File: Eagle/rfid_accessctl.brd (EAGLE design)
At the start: 50 x 40 mm, 21 parts

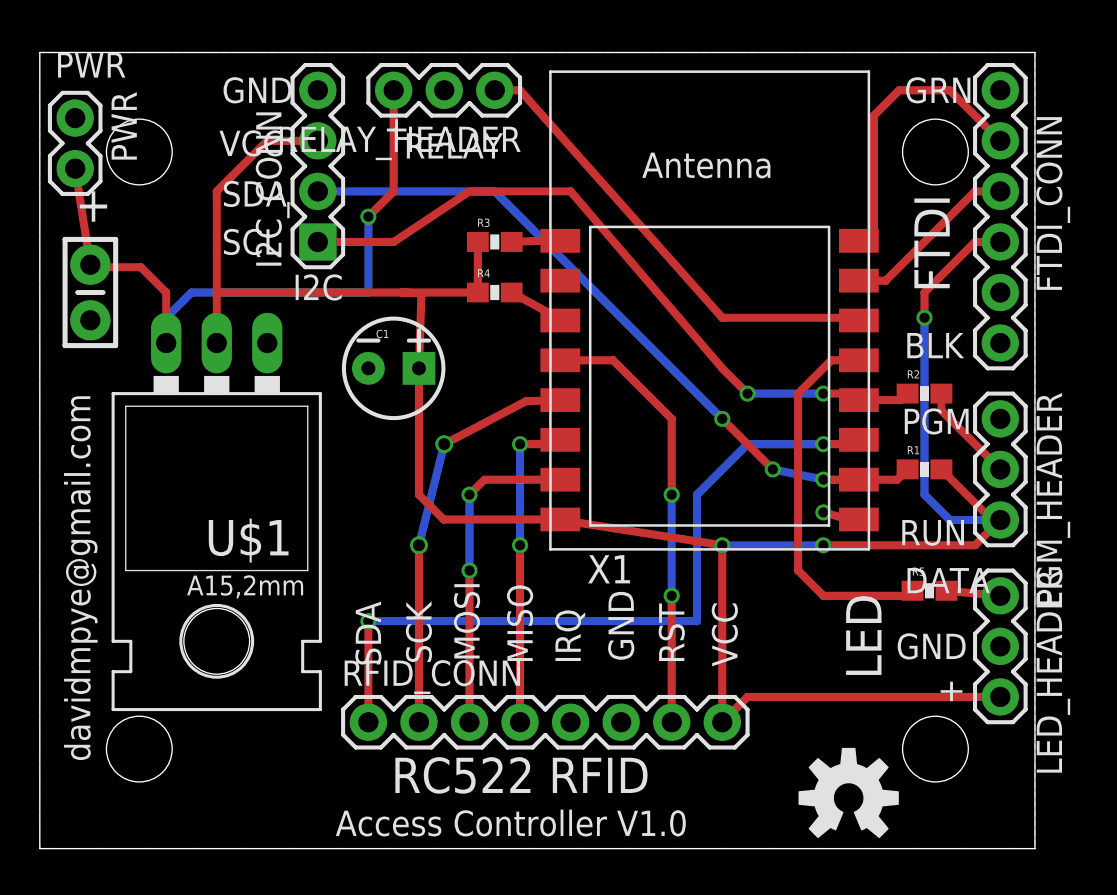
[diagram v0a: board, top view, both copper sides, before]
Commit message: Move screw holes to avoid screws fouling.
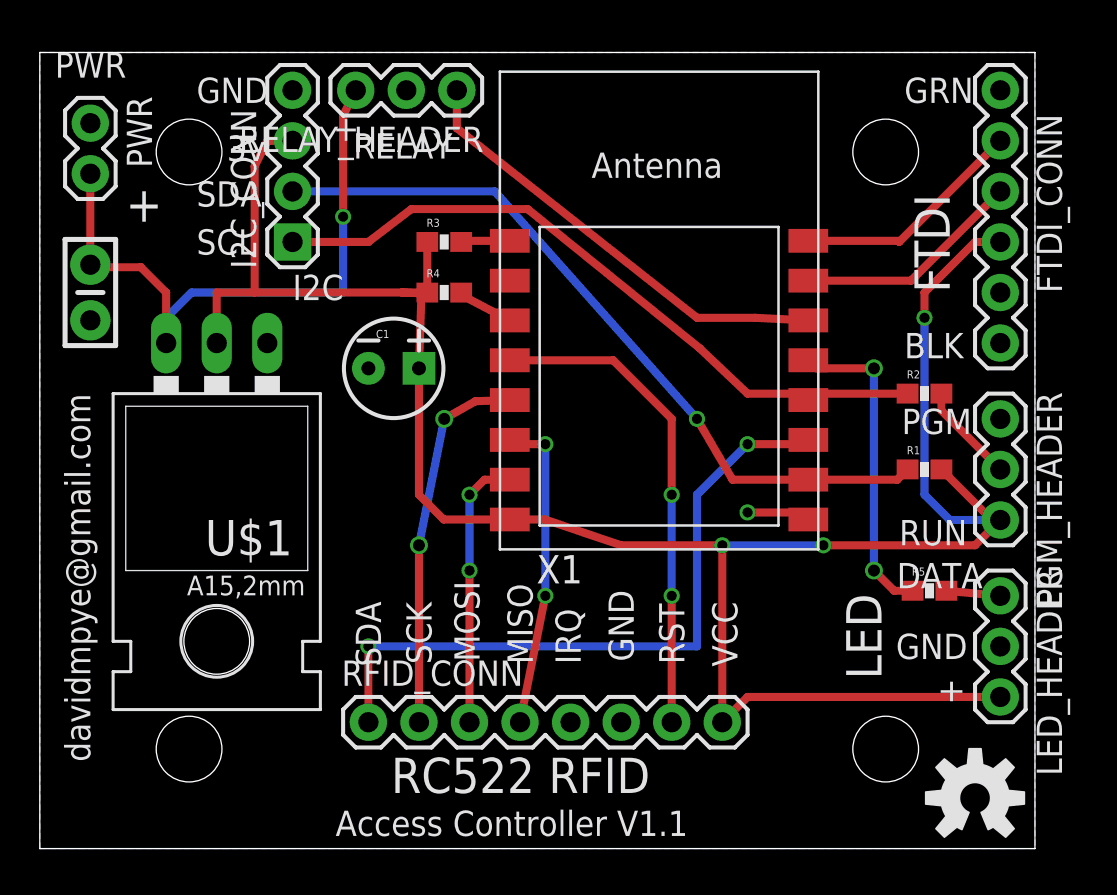
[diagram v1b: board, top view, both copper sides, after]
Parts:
- moved U$6 6.35 mm to (47.0, 2.54)
- moved X1 2.54 mm to (31.1, 26.0)
- moved R3 2.54 mm to (20.3, 30.5)
- moved R4 2.54 mm to (20.3, 27.9)
- moved U$2 2.50 mm to (42.5, 5.00)
- moved U$3 2.50 mm to (7.50, 5.00)
- moved U$4 2.50 mm to (42.5, 35.0)
- moved U$5 2.50 mm to (7.50, 35.0)
- moved RELAY_HEADER 1.91 mm to (21.0, 38.1)
- moved I2C_CONN 1.27 mm to (12.7, 30.5)
- moved PWR 0.80 mm to (2.54, 36.4)
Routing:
- net VCC: track 117.5 -> 112.8 mm
- net TXD: track 15.1 -> 11.8 mm
- net N$3: track 19.0 -> 16.0 mm, vias 0 -> 2
- net RFID_SDA: track 37.2 -> 34.7 mm
- net RFID_RST: track 22.1 -> 24.6 mm
- net RFID_MOSI: track 16.3 -> 13.8 mm
- net RXD: track 8.96 -> 11.5 mm
- net SDA: track 35.7 -> 38.0 mm, vias 3 -> 1
- net PWR_IN: track 34.5 -> 32.5 mm
- net RFID_SCK: track 20.5 -> 18.9 mm
- net GND: track 1.83 -> 3.20 mm
- net SCL: track 36.0 -> 35.1 mm, vias 2 -> 0
- net RELAY_CTL: track 23.5 -> 22.9 mm
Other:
- board text added: "3v"
- board text added: "Access Controller V1.1"
- board text removed: "Access Controller V1.0"
